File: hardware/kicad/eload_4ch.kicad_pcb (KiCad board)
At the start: 2 copper layers, 170 x 125 mm, 128 parts, among them J1 DUT+, J2 DUT-, J3 SENSE, J4 D1mini SX, J5 D1mini DX, J6 FAN, J7 NTC, J8 12V DC, Q1 IXTH75N10L2, Q2 IXTH75N10L2, Q3 IXTH75N10L2, Q4 IXTH75N10L2, Q5 FDS9926A, Q6 FDS9926A, Q7 FDS9926A, U1 TL431ID, U10 L78L05, U11 AP63205WU, U2 LM393, U3 OPA2196, U4 INA228, U5 INA228, U6 OPA2196, U7 INA228, U8 INA228, U9 DAC8565

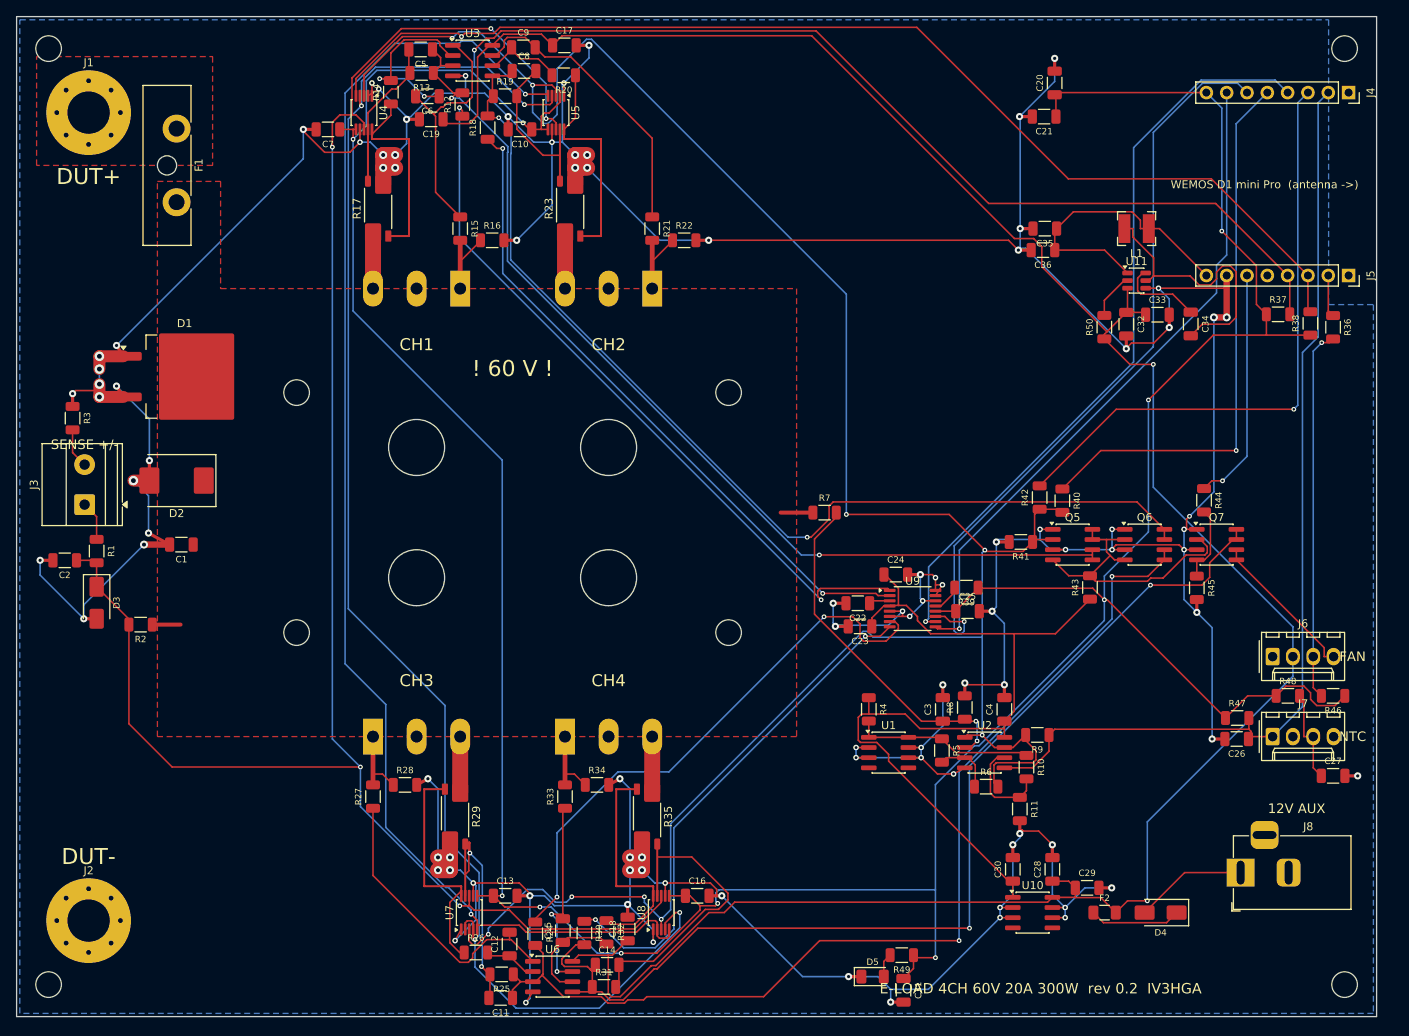
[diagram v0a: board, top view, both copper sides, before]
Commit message: rev 0.3: front panel with I2C OLED, encoder and OUTPUT button
PCF8574 expander (0x20) with INT on GPIO0, 10-pin IDC connector,
RC debounce, I2C pull-ups 2.2k, re-routed PCB (DRC/parity clean),
updated BOM, slides (front panel page) and README.

Co-Authored-By: Claude Opus 5.5 <noreply@anthropic.com>
Claude-Session: https://claude.ai/code/session_013KrwoEq2Y4F9LNKutY5RJ4
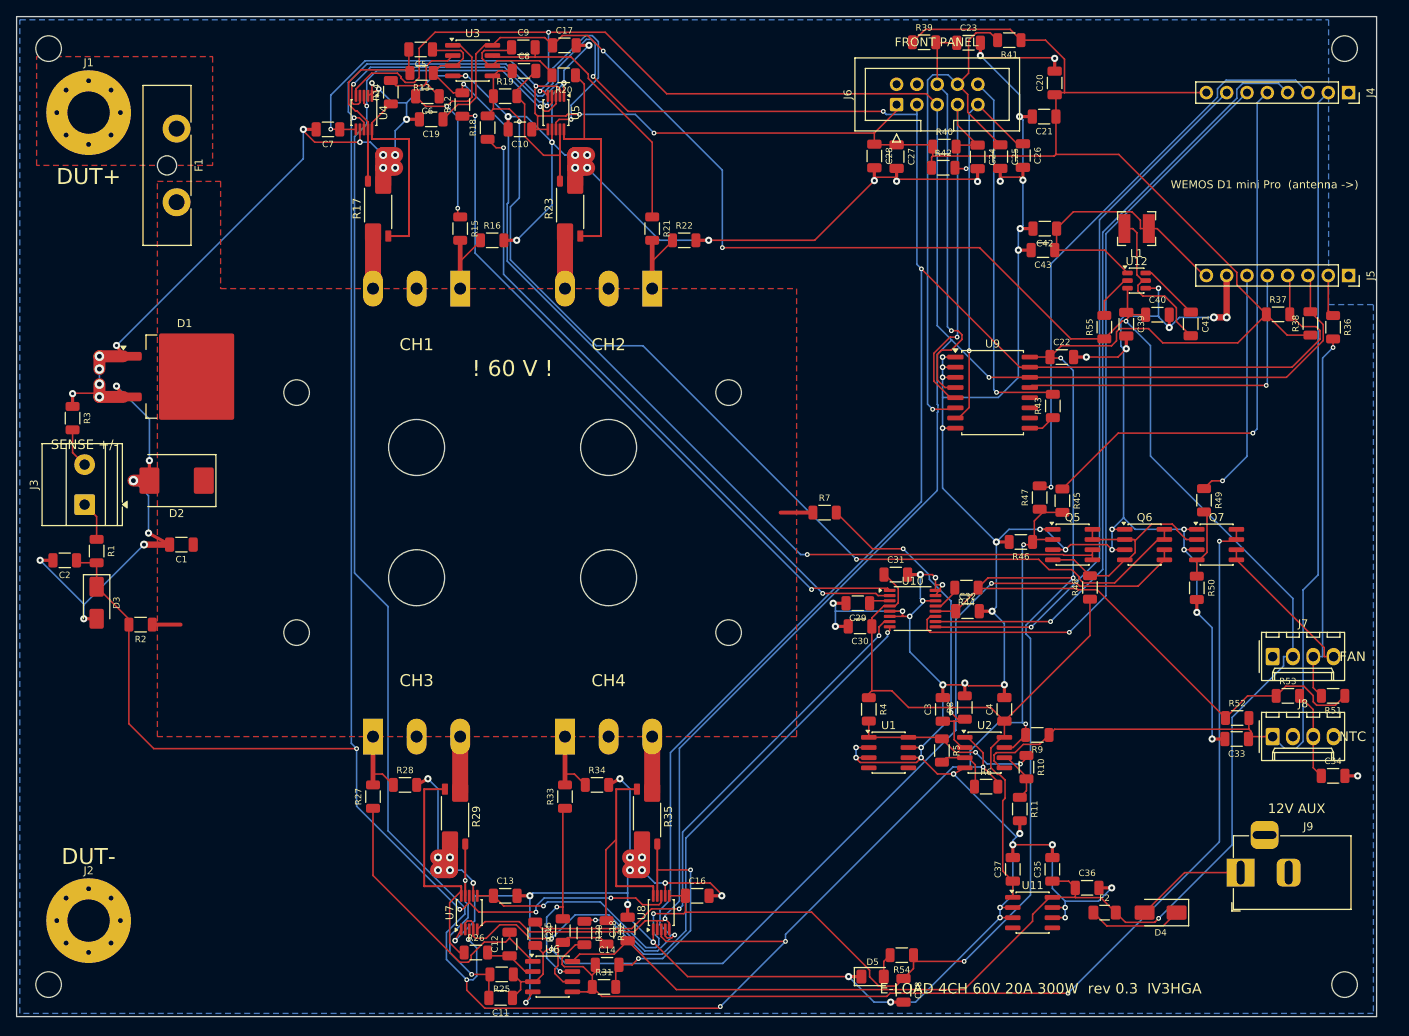
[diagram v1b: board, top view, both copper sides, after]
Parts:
- added C37: 1u, Capacitor_SMD:C_1206_3216Metric, F.Cu at (174.5, 146.6)
- added C38: 10u 25V, Capacitor_SMD:C_1206_3216Metric, F.Cu at (160.9, 161.7)
- added C39: 10u 25V, Capacitor_SMD:C_1206_3216Metric, F.Cu at (188.7, 78.4)
- added C40: 100n 50V, Capacitor_SMD:C_1206_3216Metric, F.Cu at (192.6, 77.3)
- added C41: 100n 50V, Capacitor_SMD:C_1206_3216Metric, F.Cu at (196.8, 78.4)
- added C42: 22u 10V, Capacitor_SMD:C_1206_3216Metric, F.Cu at (178.5, 66.5)
- added C43: 22u 10V, Capacitor_SMD:C_1206_3216Metric, F.Cu at (178.3, 69.2)
- added J9: 12V DC, Connector_BarrelJack:BarrelJack_Horizontal, F.Cu at (203.0, 147.0)
- added R51: 10k, Resistor_SMD:R_1206_3216Metric, F.Cu at (214.6, 124.9)
- added R52: 10k 0.1%, Resistor_SMD:R_1206_3216Metric, F.Cu at (202.6, 127.7)
- added R53: 10k 0.1%, Resistor_SMD:R_1206_3216Metric, F.Cu at (208.9, 124.9)
- added R54: 1k5, Resistor_SMD:R_1206_3216Metric, F.Cu at (160.6, 157.3)
- added R55: 100k, Resistor_SMD:R_1206_3216Metric, F.Cu at (186.0, 78.8)
- added U12: AP63205WU, Package_TO_SOT_SMD:TSOT-23-6, F.Cu at (190.0, 73.0)
- C23, C25, C26: value 100n -> 10n
- C24: value 1u -> 10n
- C27: value 100n -> 10u 25V
- C28, C32: value 10u 25V -> 100n
- C30: value 1u -> 100n
- C31: value 10u 25V -> 1u
- C33, C34: value 100n 50V -> 100n
- C35: value 22u 10V -> 10u 25V
- C36: value 22u 10V -> 100n
- J6: value FAN -> FRONT PANEL; footprint Connector_Molex:Molex_KK-254_AE-6410-04A_1x04_P2.54mm_Vertical -> Connector_IDC:IDC-Header_2x05_P2.54mm_Vertical
- J7: value NTC -> FAN
- J8: value 12V DC -> NTC; footprint Connector_BarrelJack:BarrelJack_Horizontal -> Connector_Molex:Molex_KK-254_AE-6410-04A_1x04_P2.54mm_Vertical
- R37, R38: value 4k7 -> 2k2
- R40: value 1k -> 10k
- R42: value 100k -> 10k
- R43: value 10k -> 470R
- R44: value 100R -> 10k
- R45: value 100k -> 1k
- R47: value 10k 0.1% -> 100k
- R48: value 10k 0.1% -> 10k
- R49: value 1k5 -> 100R
- U10: value L78L05 -> DAC8565; footprint Package_SO:SOIC-8_3.9x4.9mm_P1.27mm -> Package_SO:TSSOP-16_4.4x5mm_P0.65mm
- U11: value AP63205WU -> L78L05; footprint Package_TO_SOT_SMD:TSOT-23-6 -> Package_SO:SOIC-8_3.9x4.9mm_P1.27mm
- U9: value DAC8565 -> PCF8574T; footprint Package_SO:TSSOP-16_4.4x5mm_P0.65mm -> Package_SO:SOIC-16W_7.5x10.3mm_P1.27mm
- moved C27 94.7 mm to (160.0, 57.5), turned to -90 degrees
- moved C28 91.9 mm to (157.2, 57.4), turned to -90 degrees
- moved J6 83.5 mm to (160.0, 51.0), turned to 90 degrees
- moved C35 80.1 mm to (179.5, 146.6), turned to 90 degrees
- moved U11 80.1 mm to (177.0, 152.0)
- moved C36 79.9 mm to (183.8, 148.9), turned to 0 degrees
- moved C26 77.7 mm to (175.8, 57.4), turned to -90 degrees
- moved C23 74.2 mm to (169.0, 43.3), turned to 0 degrees
- moved R39 68.4 mm to (163.4, 43.2), turned to 0 degrees
- moved R49 68.3 mm to (198.4, 100.5), turned to -90 degrees
- moved R41 62.7 mm to (174.1, 42.9)
- moved C34 59.2 mm to (214.6, 134.9), turned to 0 degrees
- moved C25 57.0 mm to (173.0, 57.5), turned to -90 degrees
- moved C33 54.0 mm to (202.5, 130.3), turned to 180 degrees
- moved C24 53.2 mm to (170.1, 57.5), turned to -90 degrees
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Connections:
- C22 pad 1: /Controllo/DAC_VREF -> +3V3
- C23 pad 1: +5V -> /Controllo/FP_ENC_A
- C24 pad 1: +5V -> /Controllo/FP_ENC_B
- C25 pad 1: +3V3 -> /Controllo/FP_ENC_SW
- C26 pad 1: NTC1 -> /Controllo/FP_BTN_OUT
- C27 pad 1: /Controllo/NTC2 -> +3V3
- C28 pad 1: +12V -> +3V3
- C29 pad 1: +12V -> /Controllo/DAC_VREF
- C31 pad 1: +3V3 -> +5V
- C32 pad 1: +12V -> +3V3
- C33 pad 1: +12V -> NTC1
- C34 pad 1: /Alimentazione/BUCK_BST -> /Controllo/NTC2
- C34 pad 2: /Alimentazione/BUCK_SW -> GND
- C35 pad 1: +5V_WIFI -> +12V
- C36 pad 1: +5V_WIFI -> +12V
- J5 pad 5: unconnected-(J5-Pin_5-Pad5) -> /Controllo/EXP_INT
- J6 pad 1: GND -> +3V3
- J6 pad 2: +12V -> GND
- J6 pad 3: /Controllo/FAN_TACH -> I2C_SDA
- J6 pad 4: /Controllo/FAN_PWM -> GND
- J7 pad 1: NTC1 -> GND
- J7 pad 2: GND -> +12V
- J7 pad 3: /Controllo/NTC2 -> /Controllo/FAN_TACH
- J7 pad 4: GND -> /Controllo/FAN_PWM
- J8 pad 1: Net-(D4-A) -> NTC1
- J8 pad 3: (no net) -> /Controllo/NTC2
- R39 pad 2: /Controllo/DAC_RST -> /Controllo/FP_ENC_A
- R40 pad 1: /Controllo/ARM_DRV -> +3V3
- R40 pad 2: ARM -> /Controllo/FP_ENC_B
- R41 pad 1: ARM -> +3V3
- R41 pad 2: GND -> /Controllo/FP_ENC_SW
- R42 pad 1: ARM -> +3V3
- R42 pad 2: /Controllo/ARM_FB -> /Controllo/FP_BTN_OUT
- R43 pad 1: +5V -> /Controllo/PCF_LED
- R43 pad 2: /Controllo/CLAMP -> /Controllo/FP_LED
- R44 pad 1: /Controllo/FAN_PWM_MCU -> +3V3
- R44 pad 2: /Controllo/FAN_PWM_G -> /Controllo/DAC_RST
- R45 pad 1: /Controllo/FAN_PWM_G -> /Controllo/ARM_DRV
- R45 pad 2: GND -> ARM
- R46 pad 1: +3V3 -> ARM
- R46 pad 2: /Controllo/FAN_TACH -> GND
- R47 pad 1: +3V3 -> ARM
- R47 pad 2: NTC1 -> /Controllo/ARM_FB
- R48 pad 1: +3V3 -> +5V
- R48 pad 2: /Controllo/NTC2 -> /Controllo/CLAMP
- R49 pad 1: +3V3 -> /Controllo/FAN_PWM_MCU
- R49 pad 2: Net-(D5-A) -> /Controllo/FAN_PWM_G
- R50 pad 1: +12V -> /Controllo/FAN_PWM_G
- R50 pad 2: /Alimentazione/BUCK_EN -> GND
- U10 pad 1: +5V -> DAC_A
- U10 pad 2: GND -> DAC_B
- U10 pad 3: GND -> /Controllo/DAC_VREF
- U10 pad 4: unconnected-(U10-NC-Pad4) -> +5V
- U10 pad 5: unconnected-(U10-NC-Pad5) -> GND
- U10 pad 7: GND -> DAC_C
- U10 pad 8: +12V -> DAC_D
- U11 pad 1: +5V_WIFI -> +5V
- U11 pad 2: /Alimentazione/BUCK_EN -> GND
- U11 pad 3: +12V -> GND
- U11 pad 4: GND -> unconnected-(U11-NC-Pad4)
- U11 pad 5: /Alimentazione/BUCK_SW -> unconnected-(U11-NC-Pad5)
- U11 pad 6: /Alimentazione/BUCK_BST -> GND
- U9 pad 1: DAC_A -> GND
- U9 pad 10: /Controllo/SPI_SCK -> unconnected-(U9-P5-Pad10)
- U9 pad 11: /Controllo/SPI_MOSI -> unconnected-(U9-P6-Pad11)
- U9 pad 12: +3V3 -> unconnected-(U9-P7-Pad12)
- U9 pad 13: /Controllo/DAC_RST -> /Controllo/EXP_INT
- U9 pad 14: GND -> I2C_SCL
- U9 pad 15: GND -> I2C_SDA
- U9 pad 16: GND -> +3V3
- U9 pad 2: DAC_B -> GND
- U9 pad 3: /Controllo/DAC_VREF -> GND
- U9 pad 4: +5V -> /Controllo/FP_ENC_A
- U9 pad 5: GND -> /Controllo/FP_ENC_B
- U9 pad 6: GND -> /Controllo/FP_ENC_SW
- U9 pad 7: DAC_C -> /Controllo/FP_BTN_OUT
- U9 pad 8: DAC_D -> GND
- U9 pad 9: /Controllo/DAC_SYNC -> /Controllo/PCF_LED
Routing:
- net GND: track 772.0 -> 859.8 mm, vias 98 -> 108
- net /Controllo/FP_ENC_SW: track 0.00 -> 69.1 mm, vias 0 -> 1
- net /Controllo/FP_ENC_A: track 0.00 -> 51.2 mm, vias 0 -> 1
- net /Controllo/FP_BTN_OUT: track 0.00 -> 50.1 mm, vias 0 -> 2
- net /Controllo/FP_ENC_B: track 0.00 -> 48.7 mm, vias 0 -> 1
- net /Controllo/FP_LED: track 0.00 -> 46.6 mm, vias 0 -> 1
- net +3V3: track 444.8 -> 489.3 mm, vias 10 -> 9
- net /Controllo/EXP_INT: track 0.00 -> 43.5 mm, vias 0 -> 1
- net +5V: track 103.9 -> 80.8 mm
- net I2C_SCL: track 312.5 -> 296.8 mm, vias 3 -> 4
- net /Alimentazione/BUCK_SW: track 34.2 -> 19.9 mm
- net ARM: track 298.4 -> 310.4 mm
- net VSENSE: track 236.5 -> 247.9 mm, vias 5 -> 6
- net VSET3: track 129.9 -> 120.1 mm
- net Net-(U3A--): track 22.7 -> 13.1 mm, vias 2 -> 0
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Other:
- board text added: "E-LOAD 4CH 60V 20A 300W rev 0.3 IV3HGA"
- board text added: "FRONT PANEL"
- board text removed: "E-LOAD 4CH 60V 20A 300W rev 0.2 IV3HGA"

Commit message: Translate schematic and PCB to English
Sheets renamed (input, channels, control, power), all titles, notes,
values and board texts in English; symbol library renamed to eload.
Re-routed board: DRC with schematic parity clean.

Co-Authored-By: Claude Opus 5.5 <noreply@anthropic.com>
Claude-Session: https://claude.ai/code/session_013KrwoEq2Y4F9LNKutY5RJ4
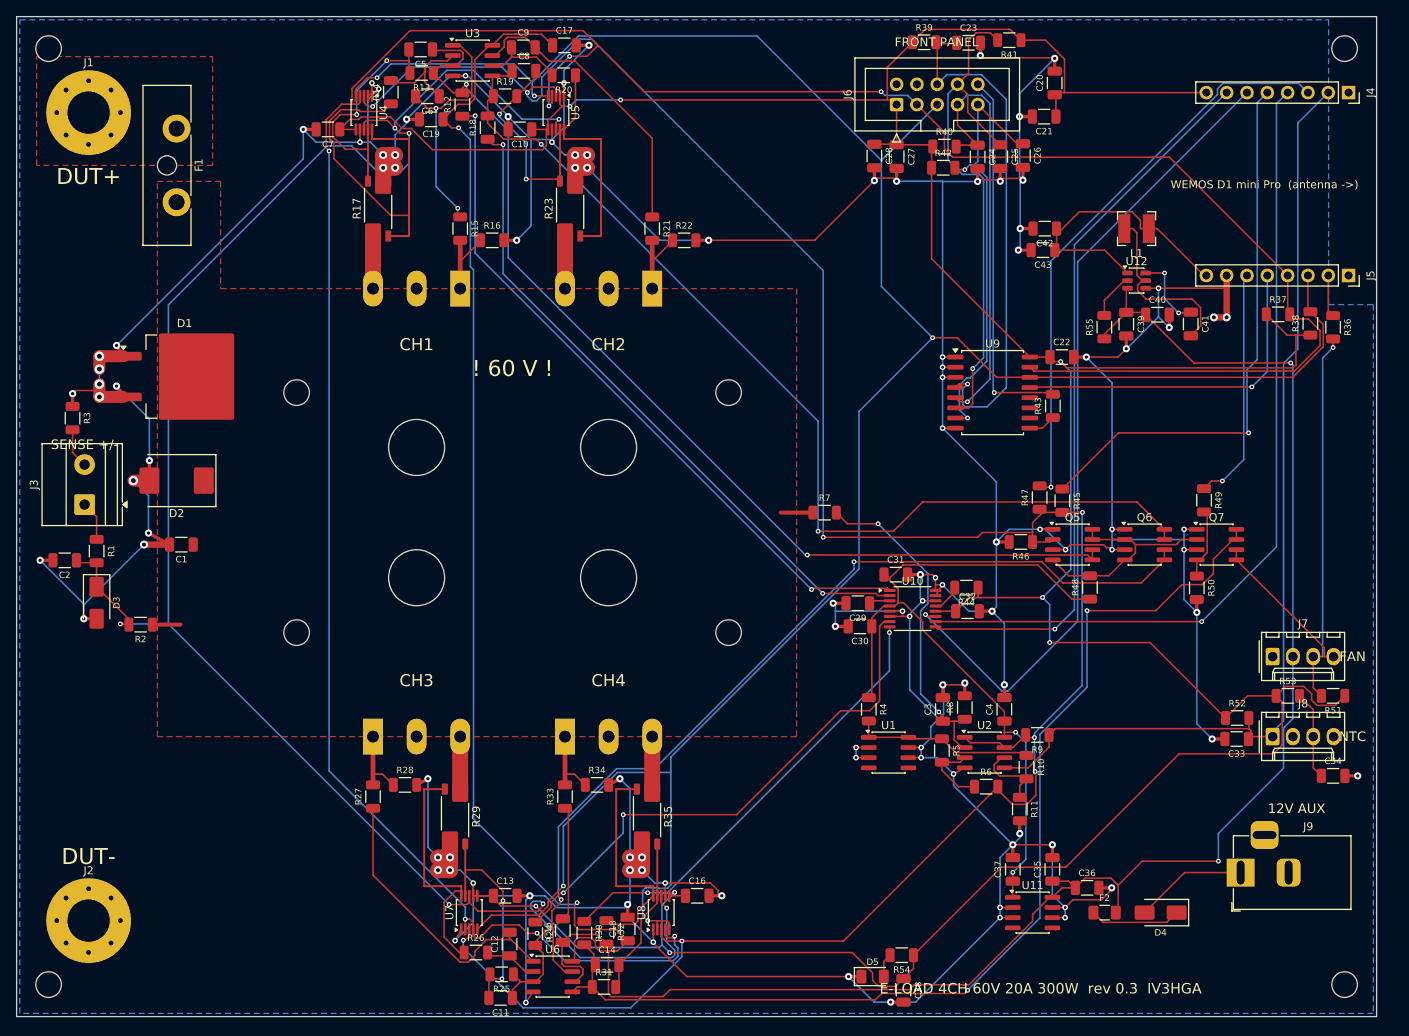
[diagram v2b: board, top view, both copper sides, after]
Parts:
- D5: value verde -> green
- J4: value D1mini SX -> D1mini L
- J5: value D1mini DX -> D1mini R
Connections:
- net /Alimentazione/BUCK_BST renamed /Power supplies/BUCK_BST
- net /Alimentazione/BUCK_EN renamed /Power supplies/BUCK_EN
- net /Alimentazione/BUCK_SW renamed /Power supplies/BUCK_SW
- net /Canali di potenza/SHN1 renamed /Power channels/SHN1
- net /Canali di potenza/SHN2 renamed /Power channels/SHN2
- net /Canali di potenza/SHN3 renamed /Power channels/SHN3
- net /Canali di potenza/SHN4 renamed /Power channels/SHN4
- net /Canali di potenza/SHP1 renamed /Power channels/SHP1
- net /Canali di potenza/SHP2 renamed /Power channels/SHP2
- net /Canali di potenza/SHP3 renamed /Power channels/SHP3
- net /Canali di potenza/SHP4 renamed /Power channels/SHP4
- net /Controllo/ARM_DRV renamed /Control/ARM_DRV
- net /Controllo/ARM_FB renamed /Control/ARM_FB
- net /Controllo/CLAMP renamed /Control/CLAMP
- net /Controllo/DAC_RST renamed /Control/DAC_RST
- net /Controllo/DAC_SYNC renamed /Control/DAC_SYNC
- net /Controllo/DAC_VREF renamed /Control/DAC_VREF
- net /Controllo/EXP_INT renamed /Control/EXP_INT
- net /Controllo/FAN_PWM renamed /Control/FAN_PWM
- net /Controllo/FAN_PWM_G renamed /Control/FAN_PWM_G
- net /Controllo/FAN_PWM_MCU renamed /Control/FAN_PWM_MCU
- net /Controllo/FAN_TACH renamed /Control/FAN_TACH
- net /Controllo/FP_BTN_OUT renamed /Control/FP_BTN_OUT
- net /Controllo/FP_ENC_A renamed /Control/FP_ENC_A
- net /Controllo/FP_ENC_B renamed /Control/FP_ENC_B
- net /Controllo/FP_ENC_SW renamed /Control/FP_ENC_SW
- net /Controllo/FP_LED renamed /Control/FP_LED
- net /Controllo/NTC2 renamed /Control/NTC2
- net /Controllo/PCF_LED renamed /Control/PCF_LED
- net /Controllo/SPI_MOSI renamed /Control/SPI_MOSI
- net /Controllo/SPI_SCK renamed /Control/SPI_SCK
- net /Controllo/WEMOS_RX renamed /Control/WEMOS_RX
- net /Ingresso e protezioni/VREF_2V5 renamed /Input and protection/VREF_2V5
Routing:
- net +12V: track 301.6 -> 343.7 mm
- net I2C_SDA: track 313.4 -> 348.4 mm
- net +3V3: track 489.3 -> 459.4 mm, vias 9 -> 8
- net /Power channels/SHP1: track 24.7 -> 46.5 mm
- net VSENSE: track 247.9 -> 232.7 mm, vias 6 -> 7
- net /Control/FP_ENC_A: track 51.2 -> 65.3 mm
- net I2C_SCL: track 296.8 -> 309.5 mm, vias 4 -> 5
- net /Power channels/SHN4: track 31.9 -> 20.0 mm, vias 2 -> 0
- net +5V: track 80.8 -> 92.1 mm, vias 0 -> 2
- net ARM: track 310.4 -> 299.1 mm, vias 9 -> 8
- net DAC_D: track 64.3 -> 56.6 mm
- net VSET4: track 142.2 -> 135.2 mm
- net /Control/SPI_SCK: track 97.7 -> 103.9 mm
- net /Power channels/SHN2: track 21.4 -> 27.5 mm, vias 0 -> 2
- net NTC1: track 128.3 -> 122.4 mm
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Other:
- board text added: "Cu SPREADER 80x70x6 (at VLOAD potential) - insulate from the cooler"
- board text added: "SP3/TR4 cooler base under the spreader"
- board text added: "Wemos antenna beyond the board edge: no copper for x > 164 mm"
- board text removed: "Antenna Wemos oltre il bordo: niente rame per x > 164 mm"
- board text removed: "Base cooler SP3/TR4 sotto lo spreader"
- board text removed: "SPREADER Cu 80x70x6 (potenziale VLOAD) - isolare dal cooler"
